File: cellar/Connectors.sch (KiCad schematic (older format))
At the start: 3 parts

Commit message: Schematic done, pending review.
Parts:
- J1: renamed from J?; footprint (none) -> Connector_PinSocket_2.54mm:PinSocket_2x20_P2.54mm_Vertical; Farnell (none) -> 2827916; Ref (none) -> 61304021821
- gave numbers to parts that had none: 2
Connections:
- net DEHUM_LEVER renamed DEHUM_LED
- net LED_ON_GND renamed LED_5V-ON_GND
- net VCOND_MEASURE renamed SWITCH0
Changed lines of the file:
@@
 $Descr A4 11693 8268
 encoding utf-8
-Sheet 2 6
+Sheet 2 8
 Title ""
 Date ""
@@
 $EndDescr
 $Comp
-L Connector:Raspberry_Pi_2_3 J?
+L Connector:Raspberry_Pi_2_3 J1
 U 1 1 5BCD8770
 P 3050 2650
-F 0 "J?" H 3650 3900 50  0000 C CNN
+F 0 "J1" H 3550 3900 50  0000 C CNN
 F 1 "Raspberry_Pi_2_3" H 2400 3900 50  0000 C CNN
-F 2 "" H 3050 2650 50  0001 C CNN
+F 2 "Connector_PinSocket_2.54mm:PinSocket_2x20_P2.54mm_Vertical" H 3050 2650 50  0001 C CNN
 F 3 "https://www.raspberrypi.org/documentation/hardware/raspberrypi/schematics/rpi_SCH_3bplus_1p0_reduced.pdf" H 3050 2650 50  0001 C CNN
+F 4 "61304021821" H 0   0   50  0001 C CNN "Ref"
+F 5 "2827916" H 3050 2650 50  0001 C CNN "Farnell"
 	1    3050 2650
 	1    0    0    -1
@@
 Wire Wire Line
 	2250 1750 2050 1750
-Text Label 4100 1750 0    50   ~ 0
-RESET_LEVER
-Text Label 4100 1850 0    50   ~ 0
-VCOND_MEASURE
-Text Label 4100 2050 0    50   ~ 0
-I2C_SDA
-Text Label 4100 2150 0    50   ~ 0
-I2C_SCL
-Text Label 4100 2350 0    50   ~ 0
-DHT22_INT
-Text Label 4100 2450 0    50   ~ 0
-HEAT_LEVER_F
-Text Label 4100 2550 0    50   ~ 0
-DEHUM_SWITCH
-Text Label 4100 2750 0    50   ~ 0
-SPI1_CE
-Text Label 4100 2850 0    50   ~ 0
-SPI0_CE
-Text Label 4100 2950 0    50   ~ 0
-SPI0_MISO
-Text Label 4100 3050 0    50   ~ 0
-SPI0_MOSI
-Text Label 4100 3150 0    50   ~ 0
-SPI0_SCLK
-Text Label 4100 3350 0    50   ~ 0
-DEHUM_LEVER_F
-Text Label 4100 3450 0    50   ~ 0
-FAN_SWITCH
-Text Label 2050 3350 2    50   ~ 0
-SERVO_ON-OFF
-Text Label 2050 3250 2    50   ~ 0
-POWER_STATE
-Text Label 2050 3150 2    50   ~ 0
-HEAT_SWITCH
-Text Label 2050 3050 2    50   ~ 0
-LIGHT_SENSOR
-Text Label 2050 2950 2    50   ~ 0
-FAN_LEVER_F
-Text Label 2050 2850 2    50   ~ 0
-WATCHDOG
-Text Label 2050 2650 2    50   ~ 0
-SPI1_SCLK
-Text Label 2050 2550 2    50   ~ 0
-SPI1_MOSI
-Text Label 2050 2450 2    50   ~ 0
-SPI1_MISO
-Text Label 2050 2250 2    50   ~ 0
-SERVO_PWM
-Text Label 2050 2150 2    50   ~ 0
-DHT22_EXT
-Text Label 2050 2050 2    50   ~ 0
-LED_RUN
-Text Label 2050 1850 2    50   ~ 0
-UART_RX_3V3
-Text Label 2050 1750 2    50   ~ 0
-UART_TX_3V3
-$Comp
-L Connector:DB25_Female_MountingHoles J?
+$Comp
+L Connector:DB25_Female_MountingHoles J2
 U 1 1 5BCD87CD
 P 6700 2600
-F 0 "J?" H 6879 2603 50  0000 L CNN
+F 0 "J2" H 6879 2603 50  0000 L CNN
 F 1 "DB25_Female" H 6879 2512 50  0000 L CNN
 F 2 "" H 6700 2600 50  0001 C CNN
@@
 Wire Wire Line
 	6400 3800 6250 3800
-Text Label 6250 1400 2    50   ~ 0
-GND
-Text Label 6250 1600 2    50   ~ 0
-UART_TX_5V
-Text Label 6250 1800 2    50   ~ 0
-UART_RX_5V
-Text Label 6250 2000 2    50   ~ 0
-+5V
-Text Label 6250 2200 2    50   ~ 0
-HEAT_LED
-Text Label 6250 2400 2    50   ~ 0
-+5V
-Text Label 6250 2600 2    50   ~ 0
-HEAT_LEVER_IN
-Text Label 6250 3000 2    50   ~ 0
-DEHUM_LEVER
-Text Label 6250 2800 2    50   ~ 0
-+3V3
-Text Label 6250 3200 2    50   ~ 0
-+5V
-Text Label 6250 3400 2    50   ~ 0
-DEHUM_LEVER_IN
-Text Label 6250 3800 2    50   ~ 0
-FAN_LED
-Text Label 6250 2900 2    50   ~ 0
-+5V
-Text Label 6250 3700 2    50   ~ 0
-+5V
-Text Label 6250 2500 2    50   ~ 0
-+5V
-Text Label 6250 3300 2    50   ~ 0
-+3V3
-Text Label 6250 1500 2    50   ~ 0
-GND
-Text Label 6250 1700 2    50   ~ 0
-GND
-Text Label 6250 1900 2    50   ~ 0
-GND
-Text Label 6250 2100 2    50   ~ 0
-+3V3
-Text Label 6250 2300 2    50   ~ 0
-RESET_LEVER
-Text Label 6250 2700 2    50   ~ 0
-LED_RUN_GND
-Text Label 6250 3100 2    50   ~ 0
-LED_ON_GND
-Text Label 6250 3500 2    50   ~ 0
-FAN_LEVER_IN
-Text Label 6250 3600 2    50   ~ 0
-+3V3
-$Comp
-L Connector:DB15_Female_MountingHoles J?
+$Comp
+L Connector:DB15_Female_MountingHoles J3
 U 1 1 5BCD8806
 P 9450 2550
-F 0 "J?" H 9605 2553 50  0000 L CNN
+F 0 "J3" H 9605 2553 50  0000 L CNN
 F 1 "DB15_Female_MountingHoles" H 9605 2462 50  0000 L CNN
 F 2 "" H 9450 2550 50  0001 C CNN
@@
 Text Label 9450 3600 2    50   ~ 0
 GND
-Text Label 9100 1850 2    50   ~ 0
-GND
-Text Label 9100 2050 2    50   ~ 0
-I2C_SDA
-Text Label 9100 2250 2    50   ~ 0
-I2C_SCL
 Wire Wire Line
 	9150 3250 9100 3250
@@
 Wire Wire Line
 	9150 2150 9100 2150
-Text Label 9100 2450 2    50   ~ 0
-SPI0_MISO
-Text Label 9100 2650 2    50   ~ 0
-SPI0_MOSI
-Text Label 9100 2850 2    50   ~ 0
-SPI0_SCLK
-Text Label 9100 3050 2    50   ~ 0
-SPI0_CE
-Text Label 9100 3250 2    50   ~ 0
-GND
-Text Label 9100 3150 2    50   ~ 0
-+3V3
-Text Label 9100 2950 2    50   ~ 0
-GND
-Text Label 9100 1950 2    50   ~ 0
-GND
-Text Label 9100 2150 2    50   ~ 0
-SPI1_MISO
-Text Label 9100 2350 2    50   ~ 0
-SPI1_MOSI
-Text Label 9100 2550 2    50   ~ 0
-SPI1_SCLK
-Text Label 9100 2750 2    50   ~ 0
-SPI1_CE
 Wire Wire Line
 	2900 1300 2900 1250
@@
 	3200 1300 3250 1300
 $Comp
-L power:+5V #PWR?
+L power:+5V #PWR01
 U 1 1 5BE0BE5A
 P 2900 1250
-F 0 "#PWR?" H 2900 1100 50  0001 C CNN
+F 0 "#PWR01" H 2900 1100 50  0001 C CNN
 F 1 "+5V" H 2915 1423 50  0000 C CNN
 F 2 "" H 2900 1250 50  0001 C CNN
@@
 $EndComp
 $Comp
-L power:+3V3 #PWR?
+L power:+3V3 #PWR03
 U 1 1 5BE0BE90
 P 3200 1250
-F 0 "#PWR?" H 3200 1100 50  0001 C CNN
+F 0 "#PWR03" H 3200 1100 50  0001 C CNN
 F 1 "+3V3" H 3215 1423 50  0000 C CNN
 F 2 "" H 3200 1250 50  0001 C CNN
@@
 	3000 4100 2950 4100
 $Comp
-L power:GND #PWR?
+L power:GND #PWR02
 U 1 1 5BE0EF14
 P 3000 4200
-F 0 "#PWR?" H 3000 3950 50  0001 C CNN
+F 0 "#PWR02" H 3000 3950 50  0001 C CNN
 F 1 "GND" H 3005 4027 50  0000 C CNN
 F 2 "" H 3000 4200 50  0001 C CNN
@@
 	1    0    0    -1
 $EndComp
+Text GLabel 2050 2050 0    50   Output ~ 0
+LED_RUN
+Text GLabel 2050 1750 0    50   Output ~ 0
+UART_TX_3V3
+Text GLabel 2050 1850 0    50   Input ~ 0
+UART_RX_3V3
+Text GLabel 2050 2150 0    50   BiDi ~ 0
+DHT22_EXT
+Text GLabel 2050 2250 0    50   Output ~ 0
+SERVO_PWM
+Text GLabel 2050 2450 0    50   Input ~ 0
+SPI1_MISO
+Text GLabel 2050 2550 0    50   Output ~ 0
+SPI1_MOSI
+Text GLabel 2050 2650 0    50   Output ~ 0
+SPI1_SCLK
+Text GLabel 2050 2850 0    50   Output ~ 0
+WATCHDOG
+Text GLabel 2050 2950 0    50   Input ~ 0
+FAN_LEVER_F
+Text GLabel 2050 3050 0    50   Input ~ 0
+LIGHT_SENSOR
+Text GLabel 2050 3150 0    50   Output ~ 0
+HEAT_SWITCH
+Text GLabel 2050 3250 0    50   Input ~ 0
+POWER_STATE
+Text GLabel 2050 3350 0    50   Output ~ 0
+SERVO_ON-OFF
+Text GLabel 4100 1750 2    50   Input ~ 0
+RESET_LEVER
+Text GLabel 4100 1850 2    50   Output ~ 0
+SWITCH0
+Text GLabel 4100 2050 2    50   BiDi ~ 0
+I2C_SDA
+Text GLabel 4100 2150 2    50   BiDi ~ 0
+I2C_SCL
+Text GLabel 4100 2350 2    50   BiDi ~ 0
+DHT22_INT
+Text GLabel 4100 2450 2    50   Input ~ 0
+HEAT_LEVER_F
+Text GLabel 4100 2550 2    50   Output ~ 0
+DEHUM_SWITCH
+Text GLabel 4100 2750 2    50   Output ~ 0
+SPI1_CE
+Text GLabel 4100 2850 2    50   Output ~ 0
+SPI0_CE
+Text GLabel 4100 2950 2    50   Input ~ 0
+SPI0_MISO
+Text GLabel 4100 3050 2    50   Output ~ 0
+SPI0_MOSI
+Text GLabel 4100 3150 2    50   Output ~ 0
+SPI0_SCLK
+Text GLabel 4100 3350 2    50   Input ~ 0
+DEHUM_LEVER_F
+Text GLabel 4100 3450 2    50   Output ~ 0
+FAN_SWITCH
+Text GLabel 6250 1400 0    50   Input ~ 0
+GND
+Text GLabel 6250 1500 0    50   Input ~ 0
+GND
+Text GLabel 6250 1600 0    50   Input ~ 0
+UART_TX_5V
+Text GLabel 6250 1700 0    50   Input ~ 0
+GND
+Text GLabel 6250 1800 0    50   Output ~ 0
+UART_RX_5V
+Text GLabel 6250 1900 0    50   Input ~ 0
+GND
+Text GLabel 6250 2000 0    50   Input ~ 0
++5V
+Text GLabel 6250 2100 0    50   Input ~ 0
++3V3
+Text GLabel 6250 2200 0    50   Input ~ 0
+HEAT_LED
+Text GLabel 6250 2300 0    50   Output ~ 0
+RESET_LEVER
+Text GLabel 6250 2400 0    50   Input ~ 0
++5V
+Text GLabel 6250 2500 0    50   Input ~ 0
++5V
+Text GLabel 6250 2600 0    50   Output ~ 0
+HEAT_LEVER_IN
+Text GLabel 6250 2700 0    50   Input ~ 0
+LED_RUN_GND
+Text GLabel 6250 2800 0    50   Input ~ 0
++3V3
+Text GLabel 6250 2900 0    50   Input ~ 0
++5V
+Text GLabel 6250 3000 0    50   Input ~ 0
+DEHUM_LED
+Text GLabel 6250 3100 0    50   Input ~ 0
+LED_5V-ON_GND
+Text GLabel 6250 3200 0    50   Input ~ 0
++5V
+Text GLabel 6250 3300 0    50   Input ~ 0
++3V3
+Text GLabel 6250 3400 0    50   Output ~ 0
+DEHUM_LEVER_IN
+Text GLabel 6250 3500 0    50   Output ~ 0
+FAN_LEVER_IN
+Text GLabel 6250 3600 0    50   Input ~ 0
++3V3
+Text GLabel 6250 3700 0    50   Input ~ 0
++5V
+Text GLabel 6250 3800 0    50   Input ~ 0
+FAN_LED
+Text GLabel 9100 1850 0    50   Input ~ 0
+GND
+Text GLabel 9100 1950 0    50   Input ~ 0
+GND
+Text GLabel 9100 2050 0    50   BiDi ~ 0
+I2C_SDA
+Text GLabel 9100 2150 0    50   Output ~ 0
+SPI1_MISO
+Text GLabel 9100 2250 0    50   BiDi ~ 0
+I2C_SCL
+Text GLabel 9100 2350 0    50   Input ~ 0
+SPI1_MOSI
+Text GLabel 9100 2450 0    50   Output ~ 0
+SPI0_MISO
+Text GLabel 9100 2550 0    50   Input ~ 0
+SPI1_SCLK
+Text GLabel 9100 2650 0    50   Input ~ 0
+SPI0_MOSI
+Text GLabel 9100 2750 0    50   Input ~ 0
+SPI1_CE
+Text GLabel 9100 2850 0    50   Input ~ 0
+SPI0_SCLK
+Text GLabel 9100 2950 0    50   Input ~ 0
+GND
+Text GLabel 9100 3050 0    50   Input ~ 0
+SPI0_CE
+Text GLabel 9100 3150 0    50   Input ~ 0
++3V3
+Text GLabel 9100 3250 0    50   Input ~ 0
+GND
+Wire Wire Line
+	3250 1300 3550 1300
+Connection ~ 3250 1300
+$Comp
+L power:PWR_FLAG #FLG0101
+U 1 1 5BE8CB1B
+P 3550 1300
+F 0 "#FLG0101" H 3550 1375 50  0001 C CNN
+F 1 "PWR_FLAG" H 3550 1474 50  0000 C CNN
+F 2 "" H 3550 1300 50  0001 C CNN
+F 3 "~" H 3550 1300 50  0001 C CNN
+	1    3550 1300
+	1    0    0    -1
+$EndComp

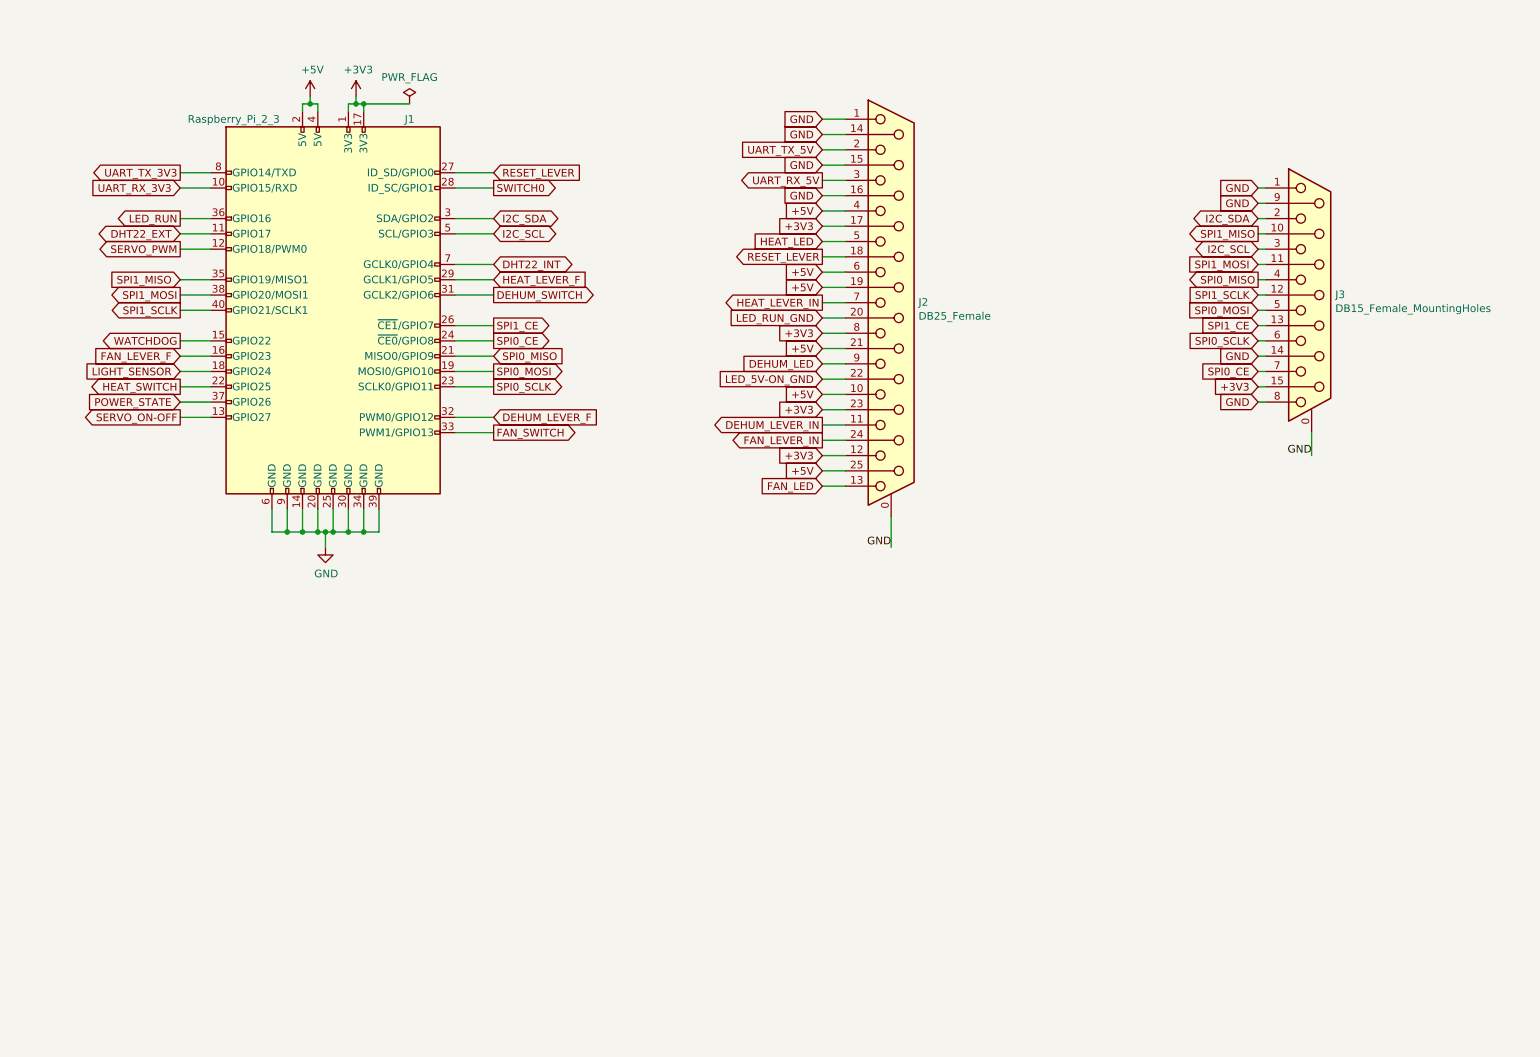
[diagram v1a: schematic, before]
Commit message: Replaced wirepads by phoenix connectors.
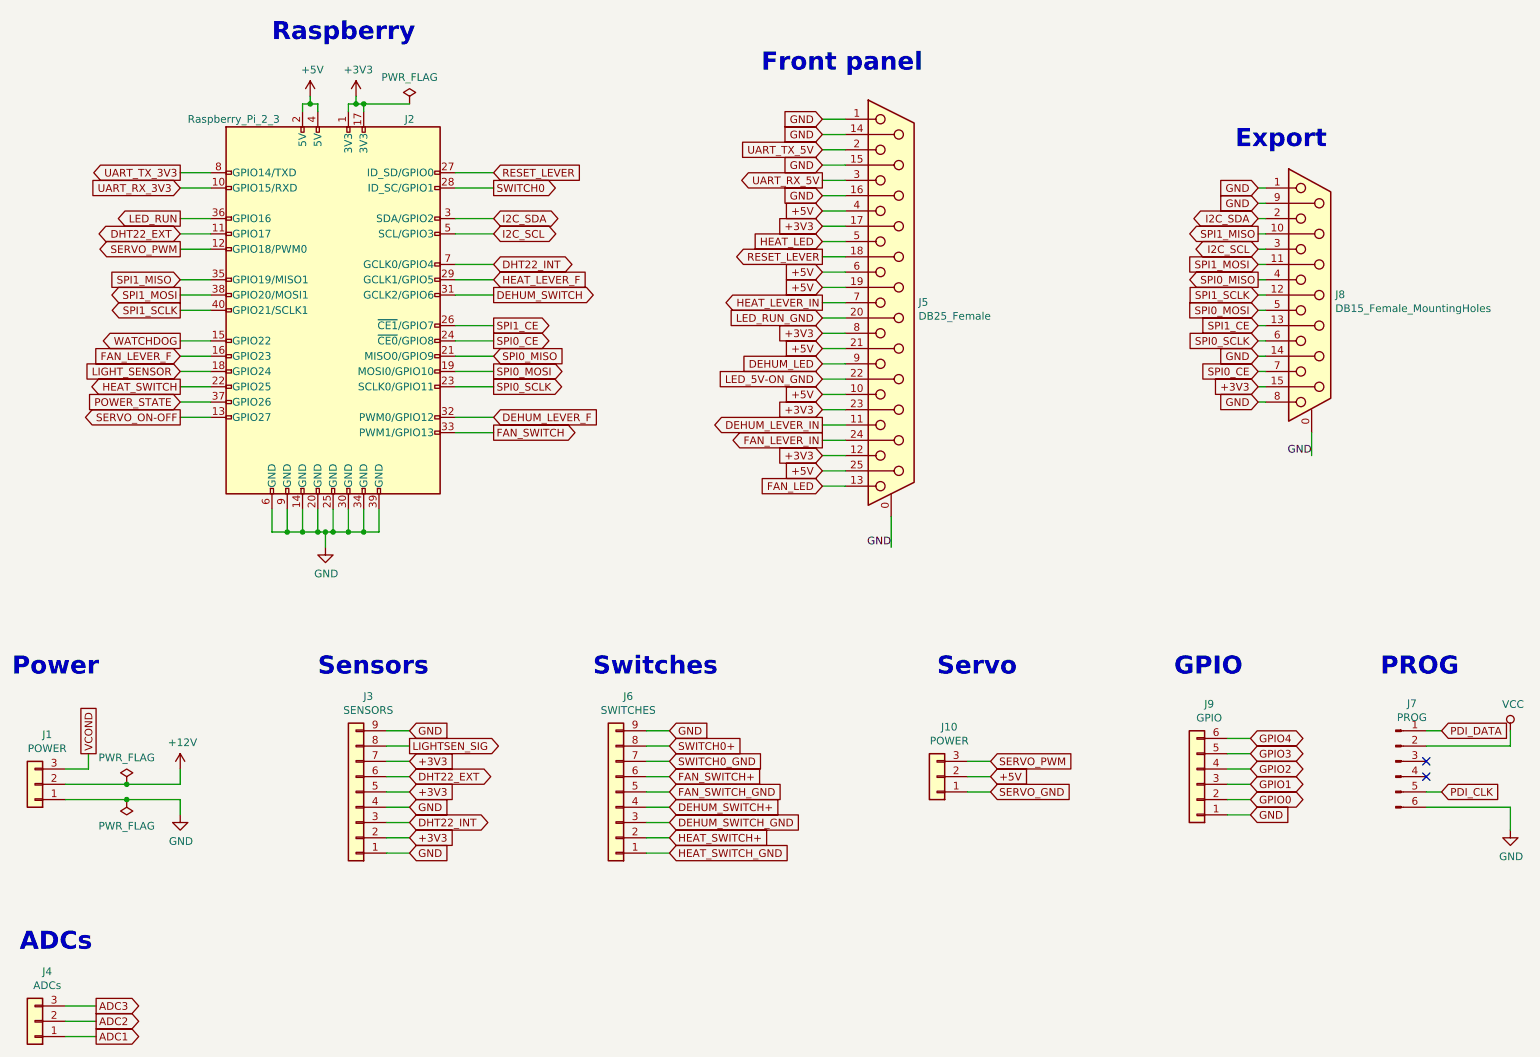
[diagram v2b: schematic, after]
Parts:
- added J1, J10: POWER, w_conn_mpt:mpt_0,5-3-2,54, symbol Connector_Generic:Conn_01x03
- added J3: SENSORS, symbol Connector_Generic:Conn_01x09
- added J4: ADCs, w_conn_mpt:mpt_0,5-3-2,54, symbol Connector_Generic:Conn_01x03
- added J6: SWITCHES, symbol Connector_Generic:Conn_01x09
- added J7: PROG, symbol Connector:Conn_01x06_Male
- added J9: GPIO, w_conn_mpt:mpt_0,5-6-2,54, symbol Connector_Generic:Conn_01x06
- J5: renamed from J2; footprint (none) -> Connectors_custom:DSUB-25_Female_Vertical_P2.77x2.84mm_MountingHoles; Farnell (none) -> 2294252; Ref (none) -> 171-025-213R001
- J8: renamed from J3; footprint (none) -> Connectors_custom:DSUB-15_Female_Vertical_P2.77x2.84mm_MountingHoles; Farnell (none) -> 2294248; Ref (none) -> 171-015-213R001
- renumbered J1 to J2
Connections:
- net +3V3: now also J3.2 (Pin_2), J3.5 (Pin_5), J3.7 (Pin_7)
- net +5V: now also J10.2 (Pin_2)
- net DHT22_EXT: now also J3.6 (Pin_6)
- net DHT22_INT: now also J3.3 (Pin_3)
- net GND: now also J1.1 (Pin_1), J3.1 (Pin_1), J3.4 (Pin_4), J3.9 (Pin_9), J6.9 (Pin_9), J7.6 (Pin_6), J9.1 (Pin_1)
- net SERVO_PWM: now also J10.3 (Pin_3)
- new net +12V: J1.2 (Pin_2)
- new net ADC1: J4.1 (Pin_1)
- new net ADC2: J4.2 (Pin_2)
- new net ADC3: J4.3 (Pin_3)
- new net DEHUM_SWITCH+: J6.4 (Pin_4)
- new net DEHUM_SWITCH_GND: J6.3 (Pin_3)
- new net FAN_SWITCH+: J6.6 (Pin_6)
- new net FAN_SWITCH_GND: J6.5 (Pin_5)
- new net GPIO0: J9.2 (Pin_2)
- new net GPIO1: J9.3 (Pin_3)
- new net GPIO2: J9.4 (Pin_4)
- new net GPIO3: J9.5 (Pin_5)
- new net GPIO4: J9.6 (Pin_6)
- new net HEAT_SWITCH+: J6.2 (Pin_2)
- new net HEAT_SWITCH_GND: J6.1 (Pin_1)
- new net LIGHTSEN_SIG: J3.8 (Pin_8)
- new net PDI_CLK: J7.5 (Pin_5)
- new net PDI_DATA: J7.1 (Pin_1)
- new net SERVO_GND: J10.1 (Pin_1)
- new net SWITCH0+: J6.8 (Pin_8)
- new net SWITCH0_GND: J6.7 (Pin_7)
- new net VCC: J7.2 (Pin_2)
- new net VCOND: J1.3 (Pin_3)
- no-connect marks 0 -> 2
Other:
- note added: "ADCs"
- note added: "Export"
- note added: "Front panel"
- note added: "GPIO"
- note added: "PROG"
- note added: "Power"
- note added: "Raspberry"
- note added: "Sensors"
- note added: "Servo"
- note added: "Switches"

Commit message: Routing in progress.
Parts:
- J10: value POWER -> SERVO
- J2: footprint Connector_PinSocket_2.54mm:PinSocket_2x20_P2.54mm_Vertical -> Connector_PinSocket_2.54mm:PinSocket_2x20_P2.54mm_Vertical_SMD
- J3, J6: footprint (none) -> w_conn_mpt:mpt_0,5-9-2,54
- J7: footprint (none) -> Connector_PinHeader_2.54mm:PinHeader_2x03_P2.54mm_Vertical
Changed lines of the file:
@@
 F 0 "J2" H 3550 3900 50  0000 C CNN
 F 1 "Raspberry_Pi_2_3" H 2400 3900 50  0000 C CNN
-F 2 "Connector_PinSocket_2.54mm:PinSocket_2x20_P2.54mm_Vertical" H 3050 2650 50  0001 C CNN
+F 2 "Connector_PinSocket_2.54mm:PinSocket_2x20_P2.54mm_Vertical_SMD" H 3050 2650 50  0001 C CNN
 F 3 "https://www.raspberrypi.org/documentation/hardware/raspberrypi/schematics/rpi_SCH_3bplus_1p0_reduced.pdf" H 3050 2650 50  0001 C CNN
-F 4 "61304021821" H 0   0   50  0001 C CNN "Ref"
-F 5 "2827916" H 3050 2650 50  0001 C CNN "Farnell"
+F 4 "2827916" H 3050 2650 50  0001 C CNN "Farnell"
+F 5 "61304021821" H 0   0   50  0001 C CNN "Ref"
 	1    3050 2650
 	1    0    0    -1
@@
 F 0 "J3" H 3120 5175 50  0000 C CNN
 F 1 "SENSORS" H 3120 5266 50  0000 C CNN
-F 2 "" H 3200 5800 50  0001 C CNN
+F 2 "w_conn_mpt:mpt_0,5-9-2,54" H 3200 5800 50  0001 C CNN
 F 3 "~" H 3200 5800 50  0001 C CNN
 F 4 "1725724" H 3200 5800 50  0001 C CNN "Ref"
@@
 F 0 "J7" H 10106 5978 50  0000 C CNN
 F 1 "PROG" H 10106 5887 50  0000 C CNN
-F 2 "" H 10000 5600 50  0001 C CNN
+F 2 "Connector_PinHeader_2.54mm:PinHeader_2x03_P2.54mm_Vertical" H 10000 5600 50  0001 C CNN
 F 3 "~" H 10000 5600 50  0001 C CNN
 	1    10000 5600
@@
 F 0 "J6" H 4820 5175 50  0000 C CNN
 F 1 "SWITCHES" H 4820 5266 50  0000 C CNN
-F 2 "" H 4900 5800 50  0001 C CNN
+F 2 "w_conn_mpt:mpt_0,5-9-2,54" H 4900 5800 50  0001 C CNN
 F 3 "~" H 4900 5800 50  0001 C CNN
 F 4 "1725724" H 4900 5800 50  0001 C CNN "Ref"
@@
 P 7000 5700
 F 0 "J10" H 6920 5375 50  0000 C CNN
-F 1 "POWER" H 6920 5466 50  0000 C CNN
+F 1 "SERVO" H 6920 5466 50  0000 C CNN
 F 2 "w_conn_mpt:mpt_0,5-3-2,54" H 7000 5700 50  0001 C CNN
 F 3 "~" H 7000 5700 50  0001 C CNN
